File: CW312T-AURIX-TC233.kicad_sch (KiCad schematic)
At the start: 24 parts, among them P1 PCIEx4 EDGE CONNECTOR, U1 TC233LP32F200NACKXUMA1, U2 LD1117SC-R

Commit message: first draft - ready for review
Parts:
- added PCB1: CE Symbol, Silkscrren_Symbols:CE-Logo_8.5x6mm_SilkScreen, symbol Silkscreen_Symbols:CE_Free
- added PCB2: Pb_Free Symbol, Silkscrren_Symbols:Pb_Free_8.0x8.0mm_SilkScreen, symbol Silkscreen_Symbols:Pb_Free
- added PCB3: UKCA symbol, Silkscrren_Symbols:UKCA-Logo_8x8mm_SilkScreen, symbol Silkscreen_Symbols:UKCA
- added PCB4: WEEE SYMBOL, Silkscrren_Symbols:WEEE-Logo_5.6x8mm_SilkScreen, symbol Silkscreen_Symbols:WEEE

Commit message: updated schematic, pcb and production files - ready for review
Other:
- note added: "pin 48 is crossed out in original schematic but still has the net label what to do"
- note removed: "pin 48 is crossed out in original schematic confirm"
- moved on the sheet: C1, C2, C3, C4, R7, R8

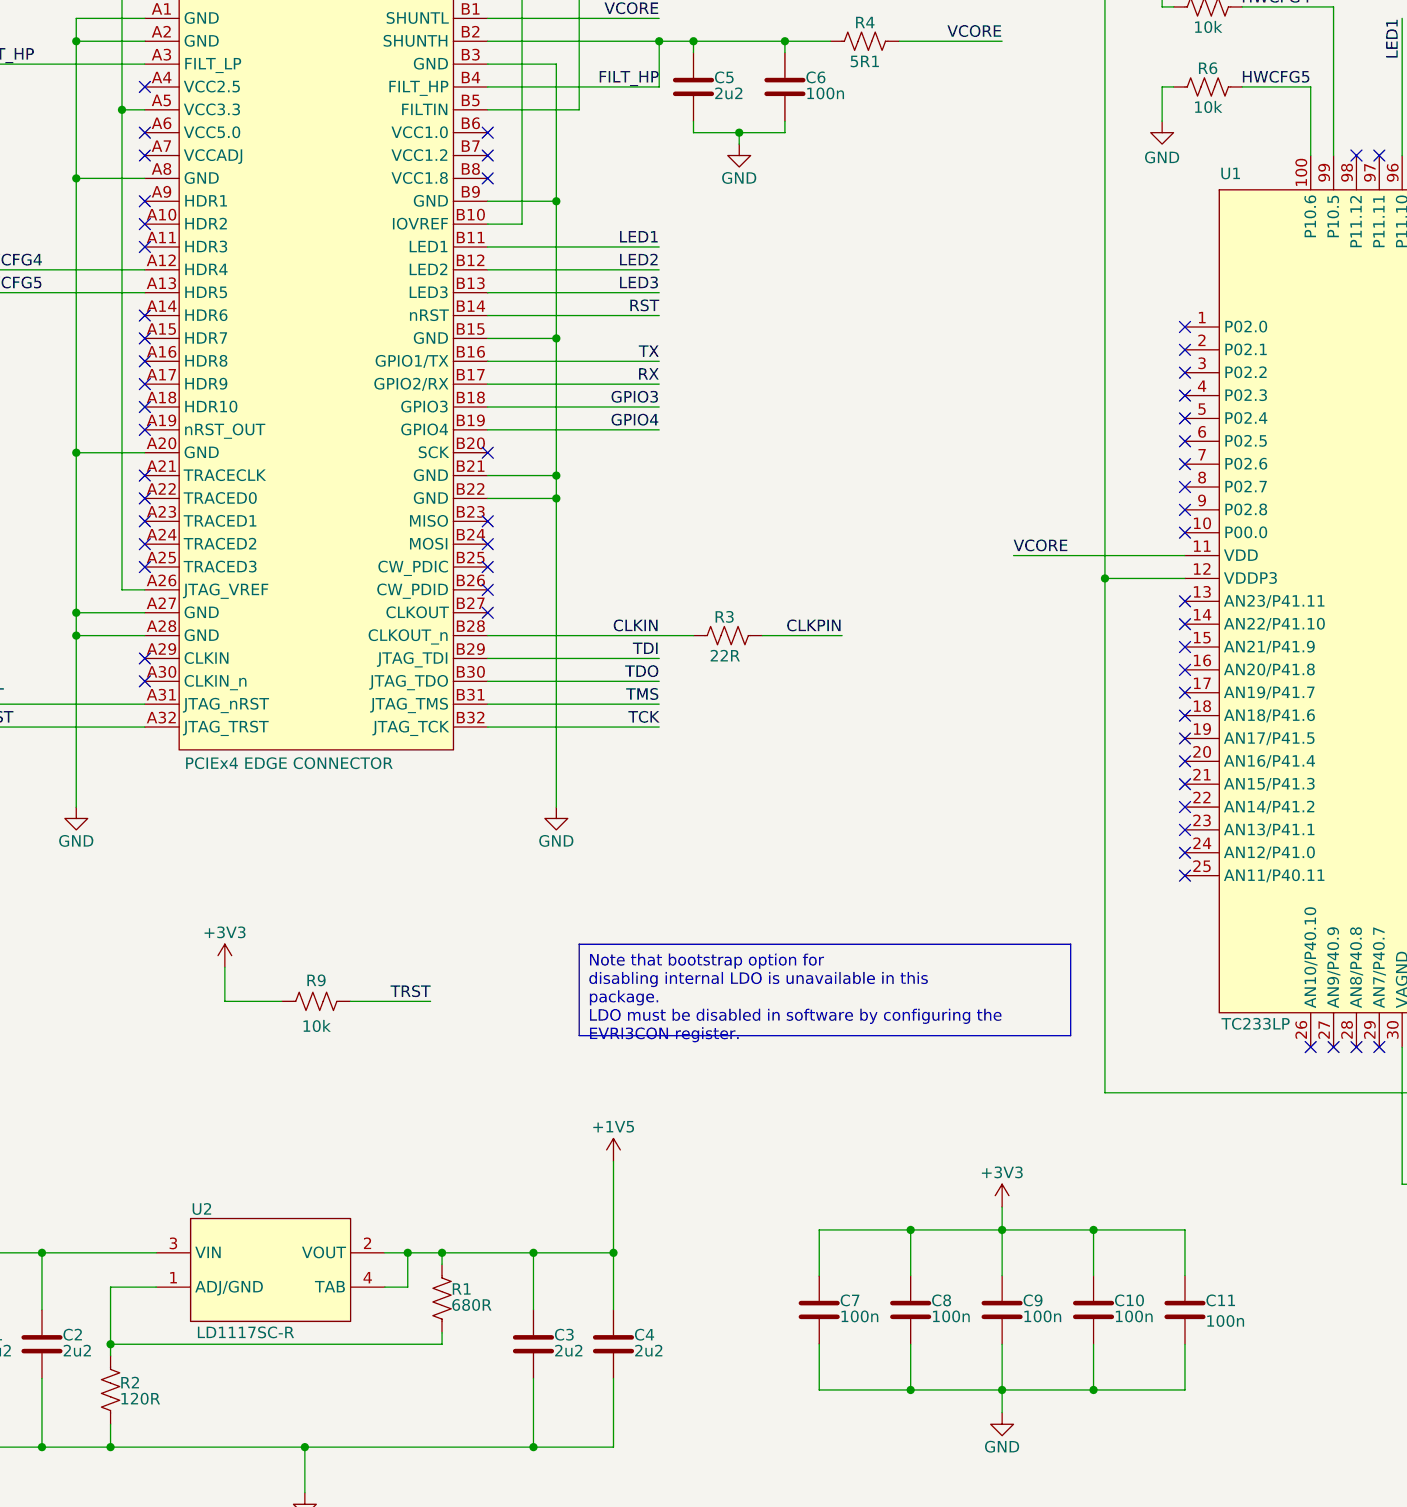
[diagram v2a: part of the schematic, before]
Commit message: updated schematic and pcb after library reorganization
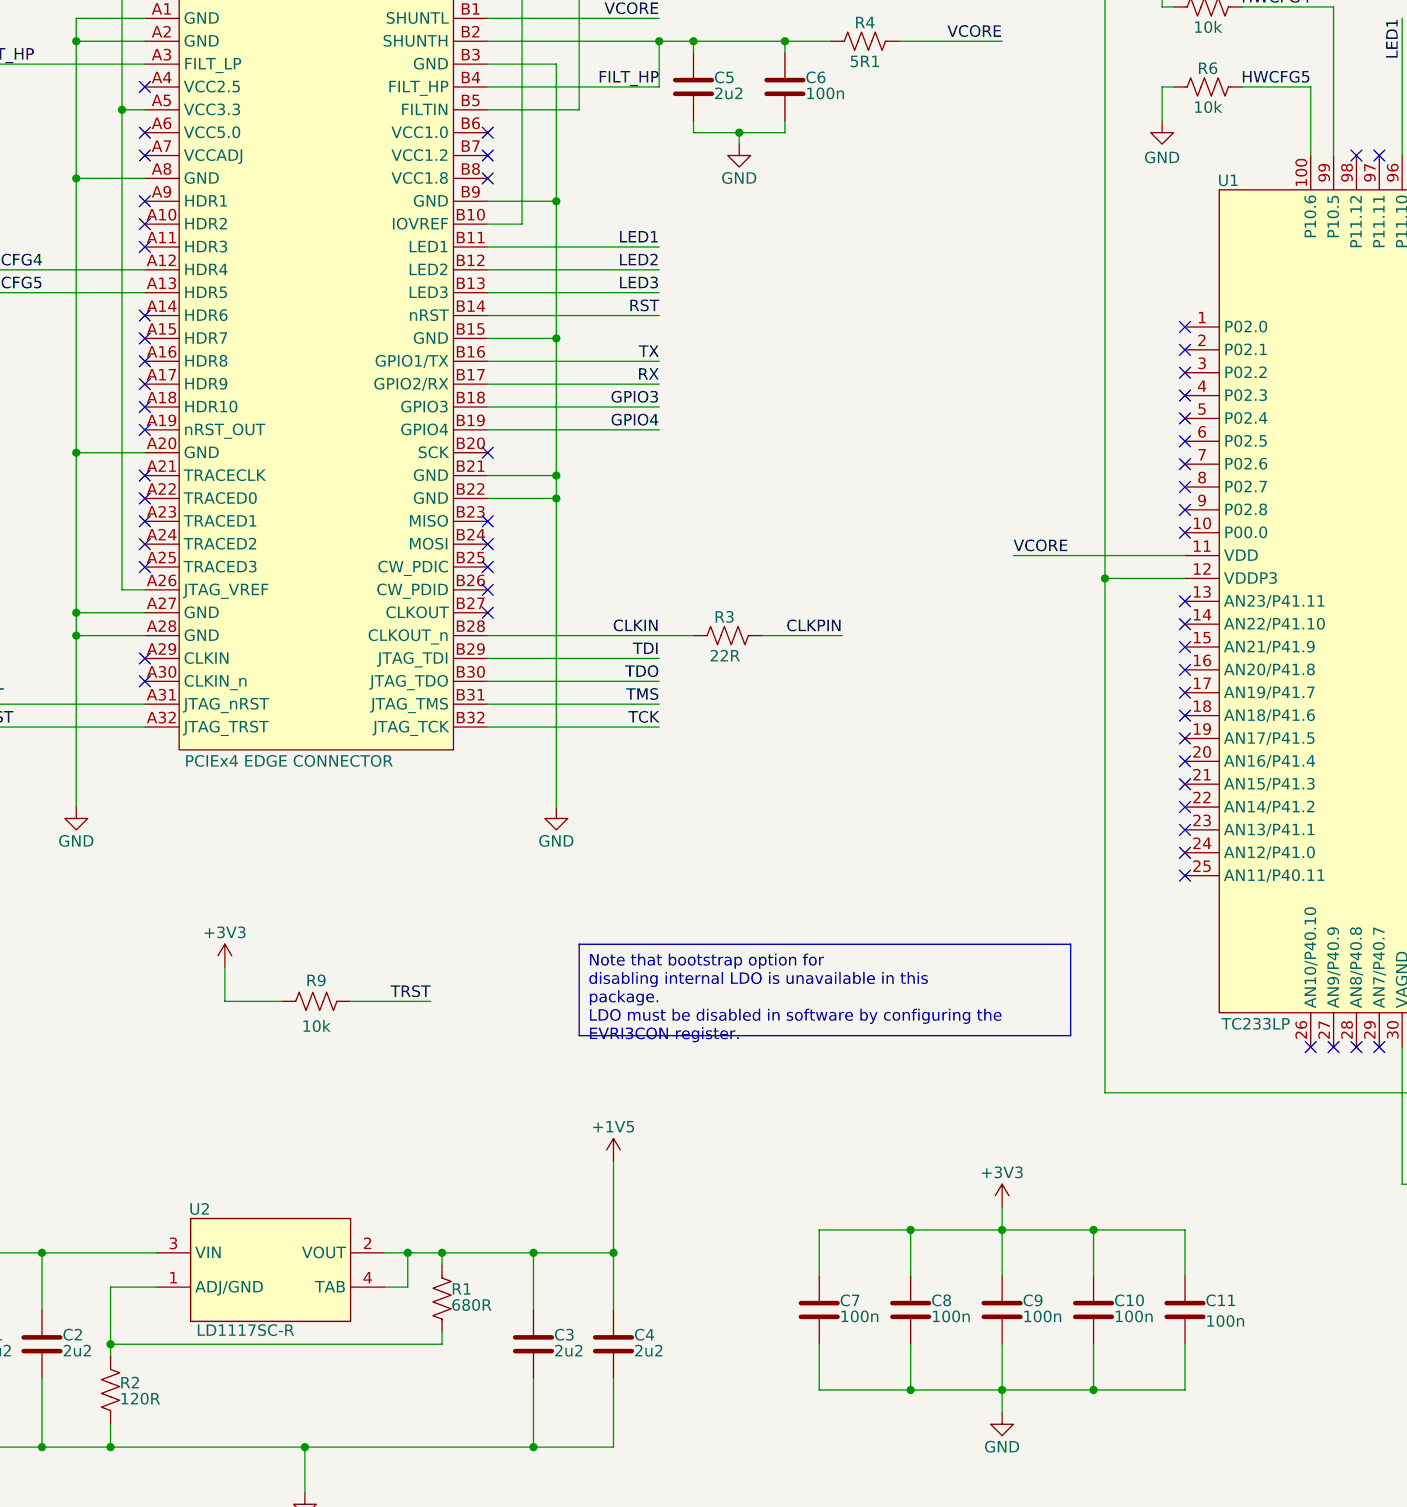
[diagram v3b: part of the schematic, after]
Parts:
- removed P1: PCIEx4 EDGE CONNECTOR, tutorial_2_library:CW312_Template, symbol tutorial_2_library:CW312T-Template
- removed U1: TC233LP32F200NACKXUMA1, Package_QFP:TQFP-100-1EP_14x14mm_P0.5mm_EP5x5mm, symbol tutorial_2_library:TC233LP32F200NACKXUMA1
- removed U2: LD1117SC-R, Package_TO_SOT_SMD:SOT-223, symbol tutorial_2_library:LD1117SC-R
- added P1: PCIEx4 EDGE CONNECTOR, tutorial_2_library:CW312_Template, symbol NAE_Connectors:CW312T-Template
- added U1: TC233LP32F200NACKXUMA1, Package_QFP:TQFP-100-1EP_14x14mm_P0.5mm_EP5x5mm, symbol NAE_Integrated_Circuits:TC233LP32F200NACKXUMA1
- added U2: LD1117SC-R, Package_TO_SOT_SMD:SOT-223, symbol NAE_Integrated_Circuits:LD1117SC-R
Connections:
- net +1V5: now also P1.B5 (FILTIN), U2.2 (VOUT), U2.4 (TAB)
- net +3V3: now also P1.A26 (JTAG_VREF), P1.A5 (VCC3.3), P1.B10 (IOVREF), U1.12 (VDDP3), U1.31 (VAREF), U1.33 (VDDM), U1.47 (VDDP3), U1.55 (VDDP3), U1.86 (VDDP3), U2.3 (VIN)
- net CLKIN: now also P1.B28 (CLKOUT_n)
- net CLKPIN: now also U1.53 (XTAL1)
- net FILT_HP: now also P1.A3 (FILT_LP), P1.B2 (SHUNTH), P1.B4 (FILT_HP)
- net GND: now also P1.A1 (GND), P1.A2 (GND), P1.A20 (GND), P1.A27 (GND), P1.A28 (GND), P1.A8 (GND), P1.B15 (GND), P1.B21 (GND), P1.B22 (GND), P1.B3 (GND), P1.B9 (GND), U1.101 (PAD), U1.30 (VAGND), U1.32 (VSSM)
- net GPIO3: now also P1.B18 (GPIO3), U1.83 (P14.3)
- net GPIO4: now also P1.B19 (GPIO4), U1.84 (P14.4)
- net HWCFG4: now also P1.A12 (HDR4), U1.99 (P10.5)
- net HWCFG5: now also P1.A13 (HDR5), U1.100 (P10.6)
- net LED1: now also P1.B11 (LED1), U1.96 (P11.10)
- net LED2: now also P1.B12 (LED2), U1.94 (P11.9)
- net LED3: now also P1.B13 (LED3), U1.92 (P11.3)
- net RST: now also P1.A31 (JTAG_nRST), P1.B14 (nRST), U1.66 (~{PORST})
- net RX: now also P1.B17 (GPIO2/RX), U1.79 (P15.3)
- net TCK: now also P1.B32 (JTAG_TCK), U1.63 (TCK/DAP0)
- net TDI: now also P1.B29 (JTAG_TDI), U1.59 (P21.6/TDI)
- net TDO: now also P1.B30 (JTAG_TDO), U1.61 (P21.7/TDO/DAP2)
- net TMS: now also P1.B31 (JTAG_TMS), U1.60 (TMS/DAP1)
- net TRST: now also P1.A32 (JTAG_TRST), U1.62 (~{TRST})
- net TX: now also P1.B16 (GPIO1/TX), U1.78 (P15.2)
- net VCORE: now also P1.B1 (SHUNTL), U1.11 (VDD), U1.48 (VDD), U1.52 (VDD), U1.68 (VDD)
- net at R7.1: now also U1.64 (P20.2/~{TESTMODE})
- net at C12.1: now also U1.49 (VC_AP0)
- net at C12.2: now also U1.50 (VC_AP1)
- net at R1.1, R2.2: now also U2.1 (ADJ/GND)
